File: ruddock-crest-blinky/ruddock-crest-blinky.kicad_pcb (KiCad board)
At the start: 2 copper layers, 38.1 x 45.7 mm, 35 parts, among them J1 JST PH, Q1 DMN2058UW, SW1 JS102011JCQN, SW2 PTS 647 SK38 SMTR2 LFS, U1 ATtiny85-20SU, U2 74HC595

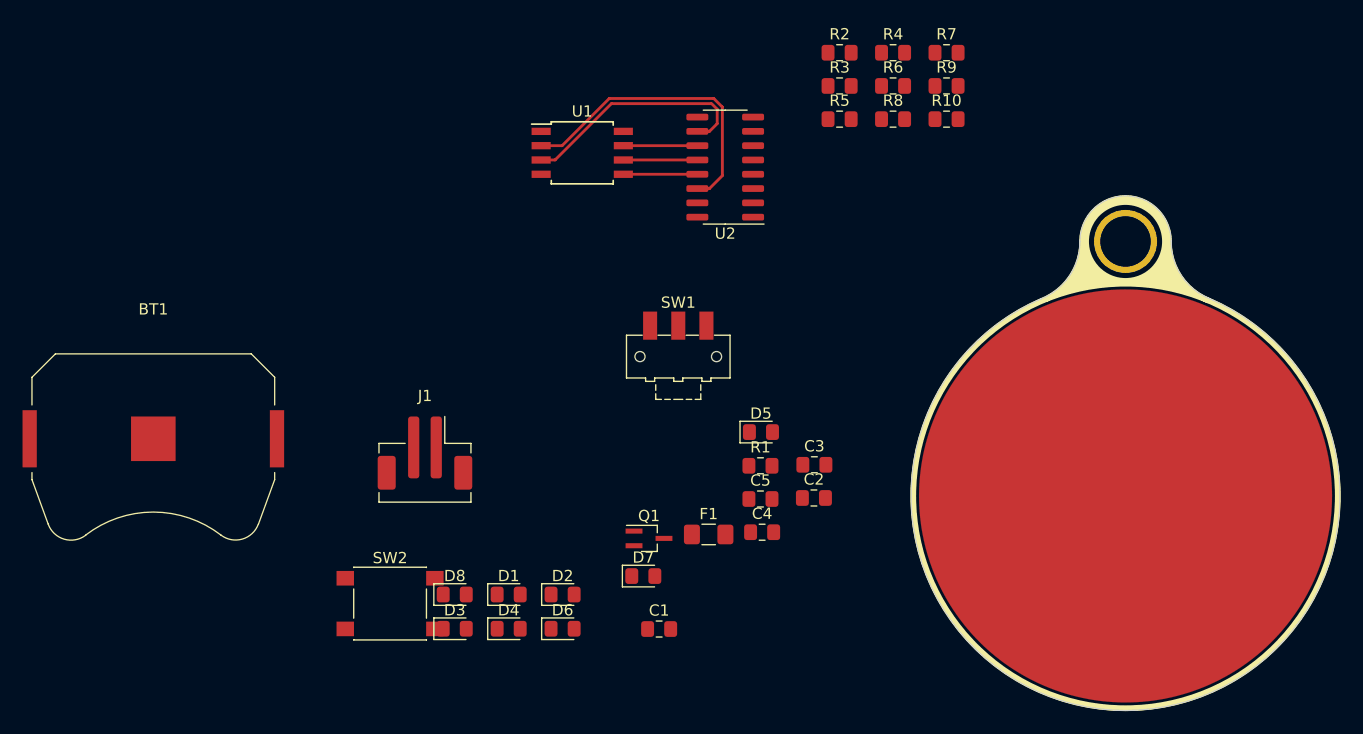
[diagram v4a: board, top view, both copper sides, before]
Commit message: Definitely not driving 8 blue LEDs off single CR2032
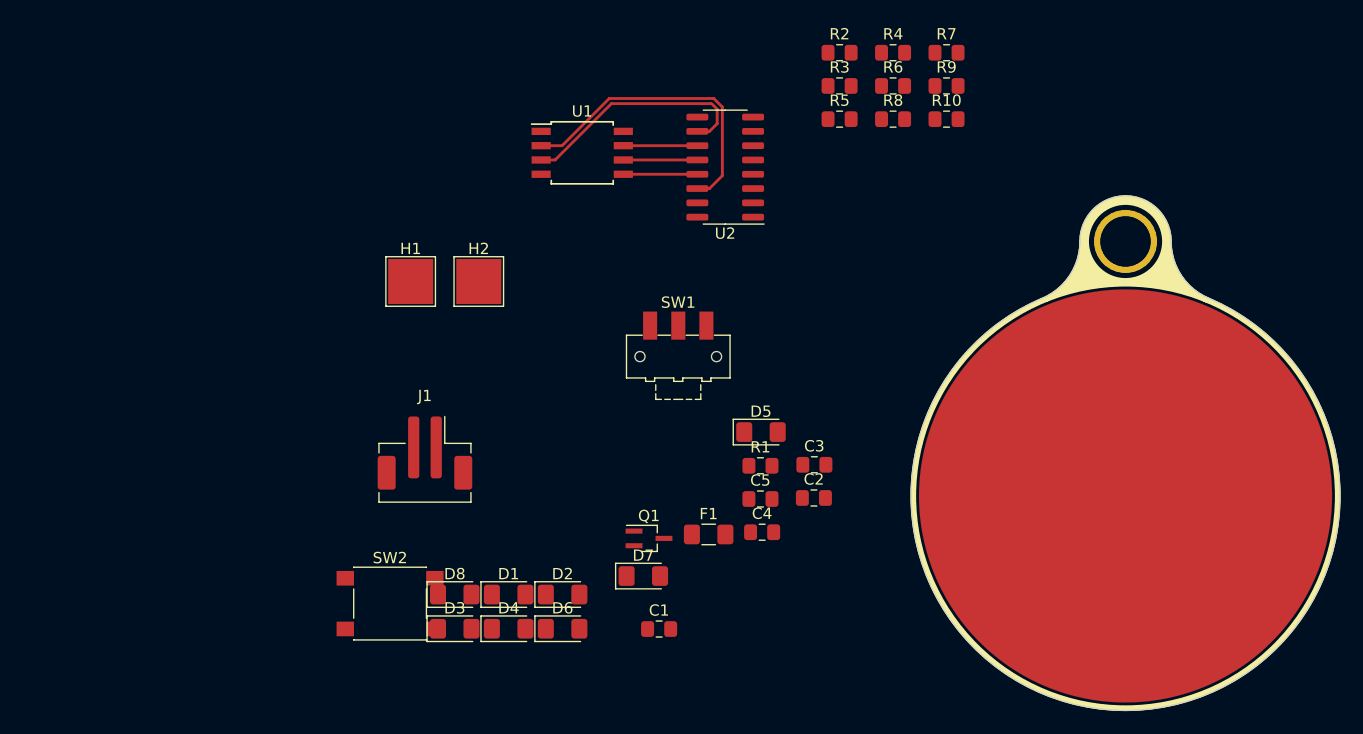
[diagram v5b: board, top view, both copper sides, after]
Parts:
- removed BT1: CR2032, Battery:BatteryHolder_Keystone_3034_1x20mm
- added H1: BAT_POS, TestPoint:TestPoint_Pad_4.0x4.0mm, F.Cu at (77.5, 88.9)
- added H2: BAT_NEG, TestPoint:TestPoint_Pad_4.0x4.0mm, F.Cu at (83.5, 88.9)
- D1, D2, D3, D4, D5, D6, D7, D8: value BLUE -> 150120BS75000; footprint LED_SMD:LED_0805_2012Metric_Pad1.15x1.40mm_HandSolder -> LED_SMD:LED_1206_3216Metric_Pad1.42x1.75mm_HandSolder
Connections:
- net Net-(BT1-Pad1) renamed /BAT+
- net Net-(BT1-Pad2) renamed /BAT-

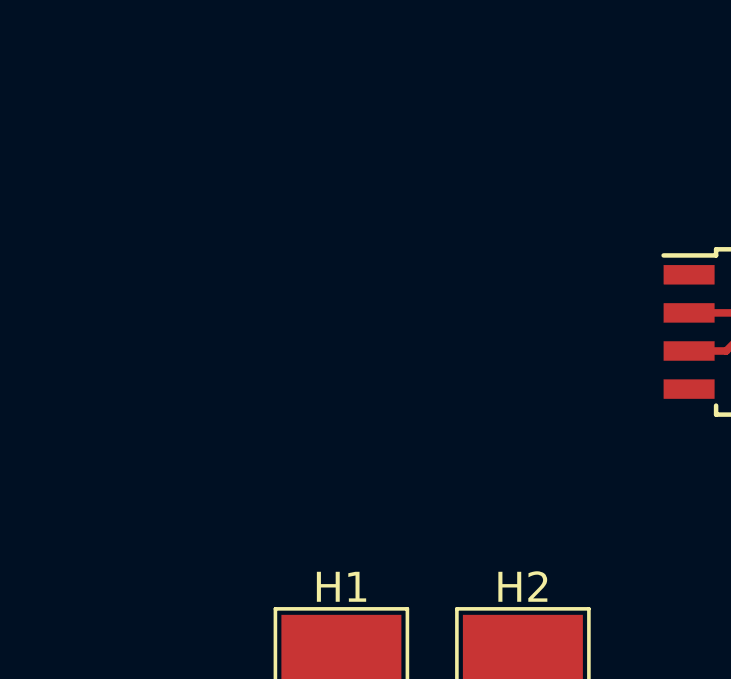
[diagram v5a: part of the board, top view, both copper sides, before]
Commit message: Add symbols for mounting hole and crest copper
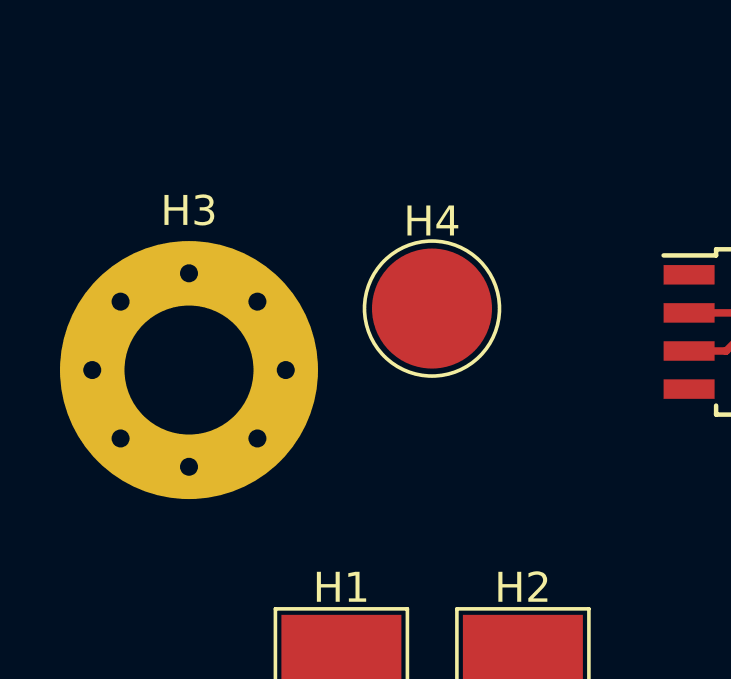
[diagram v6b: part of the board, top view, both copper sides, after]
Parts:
- added H3: KEYHOLE, MountingHole:MountingHole_4.3mm_M4_Pad_Via, F.Cu at (72.4, 78.7)
- added H4: CREST, TestPoint:TestPoint_Pad_D4.0mm, F.Cu at (80.5, 76.7)
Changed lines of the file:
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@@
     (tracks 19)
     (zones 0)
-    (modules 36)
-    (nets 31)
+    (modules 38)
+    (nets 33)
   )
   (page A)
@@
     (mod_text_size 1 1)
     (mod_text_width 0.15)
-    (pad_size 5.6 5.6)
-    (pad_drill 4.5)
+    (pad_size 7.366 7.366)
+    (pad_drill 5.334)
     (pad_to_mask_clearance 0.2)
     (solder_mask_min_width 0.25)
@@
   (net 29 /BAT+)
   (net 30 /BAT-)
+  (net 31 "Net-(H3-Pad1)")
+  (net 32 "Net-(H4-Pad1)")
   (net_class Default "This is the default net class."
     (clearance 0.2032)
@@
     (add_net "Net-(D8-Pad2)")
     (add_net "Net-(F1-Pad2)")
+    (add_net "Net-(H3-Pad1)")
+    (add_net "Net-(H4-Pad1)")
     (add_net "Net-(R1-Pad2)")
     (add_net "Net-(R2-Pad1)")
@@
     (add_net VCC)
   )
+  (module TestPoint:TestPoint_Pad_D4.0mm (layer F.Cu)
+    (at 80.49 76.69)
+    (descr "SMD pad as test Point, diameter 4.0mm")
+    (tags "test point SMD pad")
+    (attr virtual)
+    (fp_text reference H4 (at 0 -2.898) (layer F.SilkS)
+      (effects (font (size 1 1) (thickness 0.15)))
+    )
+    (fp_text value CREST (at 0 3.1) (layer F.Fab)
+      (effects (font (size 1 1) (thickness 0.15)))
+    )
+    (fp_circle (center 0 0) (end 0 2.25) (layer F.SilkS) (width 0.12))
+    (fp_circle (center 0 0) (end 2.5 0) (layer F.CrtYd) (width 0.05))
+    (fp_text user %R (at 0 -2.9) (layer F.Fab)
+      (effects (font (size 1 1) (thickness 0.15)))
+    )
+    (pad 1 smd circle (at 0 0) (size 4 4) (layers F.Cu F.Mask)
+      (net 32 "Net-(H4-Pad1)"))
+  )
+  (module MountingHole:MountingHole_4.3mm_M4_Pad_Via (layer F.Cu)
+    (at 72.39 78.74)
+    (descr "Mounting Hole 4.3mm, M4")
+    (tags "mounting hole 4.3mm m4")
+    (attr virtual)
+    (fp_text reference H3 (at 0 -5.3) (layer F.SilkS)
+      (effects (font (size 1 1) (thickness 0.15)))
+    )
+    (fp_text value KEYHOLE (at 0 5.3) (layer F.Fab)
+      (effects (font (size 1 1) (thickness 0.15)))
+    )
+    (fp_circle (center 0 0) (end 4.55 0) (layer F.CrtYd) (width 0.05))
+    (fp_circle (center 0 0) (end 4.3 0) (layer Cmts.User) (width 0.15))
+    (fp_text user %R (at 0.3 0) (layer F.Fab)
+      (effects (font (size 1 1) (thickness 0.15)))
+    )
+    (pad 1 thru_hole circle (at 2.280419 -2.280419) (size 0.9 0.9) (drill 0.6) (layers *.Cu *.Mask)
+      (net 31 "Net-(H3-Pad1)"))
+    (pad 1 thru_hole circle (at 0 -3.225) (size 0.9 0.9) (drill 0.6) (layers *.Cu *.Mask)
+      (net 31 "Net-(H3-Pad1)"))
+    (pad 1 thru_hole circle (at -2.280419 -2.280419) (size 0.9 0.9) (drill 0.6) (layers *.Cu *.Mask)
+      (net 31 "Net-(H3-Pad1)"))
+    (pad 1 thru_hole circle (at -3.225 0) (size 0.9 0.9) (drill 0.6) (layers *.Cu *.Mask)
+      (net 31 "Net-(H3-Pad1)"))
+    (pad 1 thru_hole circle (at -2.280419 2.280419) (size 0.9 0.9) (drill 0.6) (layers *.Cu *.Mask)
+      (net 31 "Net-(H3-Pad1)"))
+    (pad 1 thru_hole circle (at 0 3.225) (size 0.9 0.9) (drill 0.6) (layers *.Cu *.Mask)
+      (net 31 "Net-(H3-Pad1)"))
+    (pad 1 thru_hole circle (at 2.280419 2.280419) (size 0.9 0.9) (drill 0.6) (layers *.Cu *.Mask)
+      (net 31 "Net-(H3-Pad1)"))
+    (pad 1 thru_hole circle (at 3.225 0) (size 0.9 0.9) (drill 0.6) (layers *.Cu *.Mask)
+      (net 31 "Net-(H3-Pad1)"))
+    (pad 1 thru_hole circle (at 0 0) (size 8.6 8.6) (drill 4.3) (layers *.Cu *.Mask)
+      (net 31 "Net-(H3-Pad1)"))
+  )
   (module TestPoint:TestPoint_Pad_4.0x4.0mm (layer F.Cu)

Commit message: Add labels to MCU pins
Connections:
- net Net-(C5-Pad1) renamed /USER
- net Net-(R1-Pad2) renamed /RESET
- net Net-(U1-Pad2) renamed /SER
- net Net-(U1-Pad5) renamed /~OE
- net Net-(U1-Pad6) renamed /RCLK
- net Net-(U1-Pad7) renamed /SRCLK

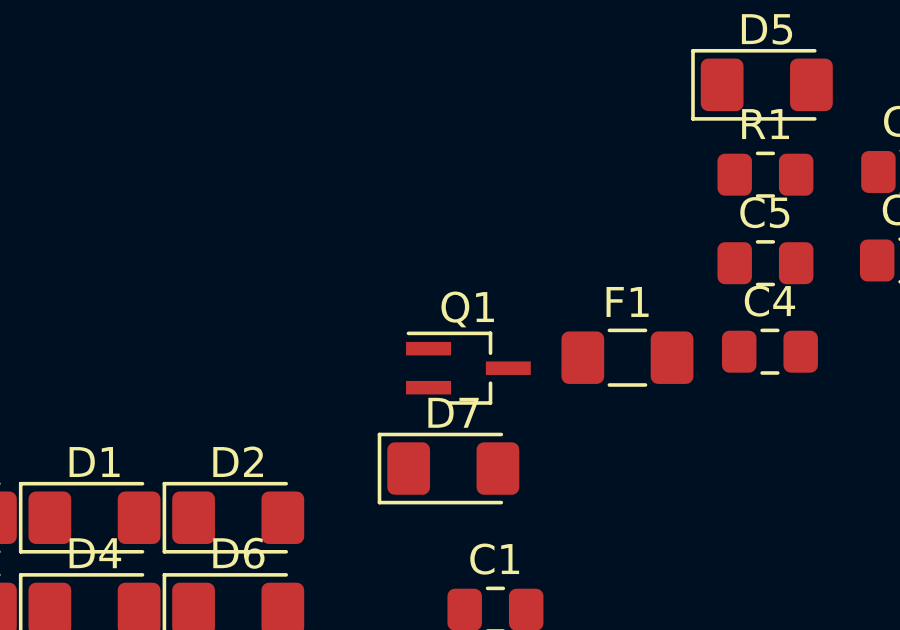
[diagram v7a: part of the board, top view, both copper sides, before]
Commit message: Replace MOSFET with SOT-23 for easier soldering
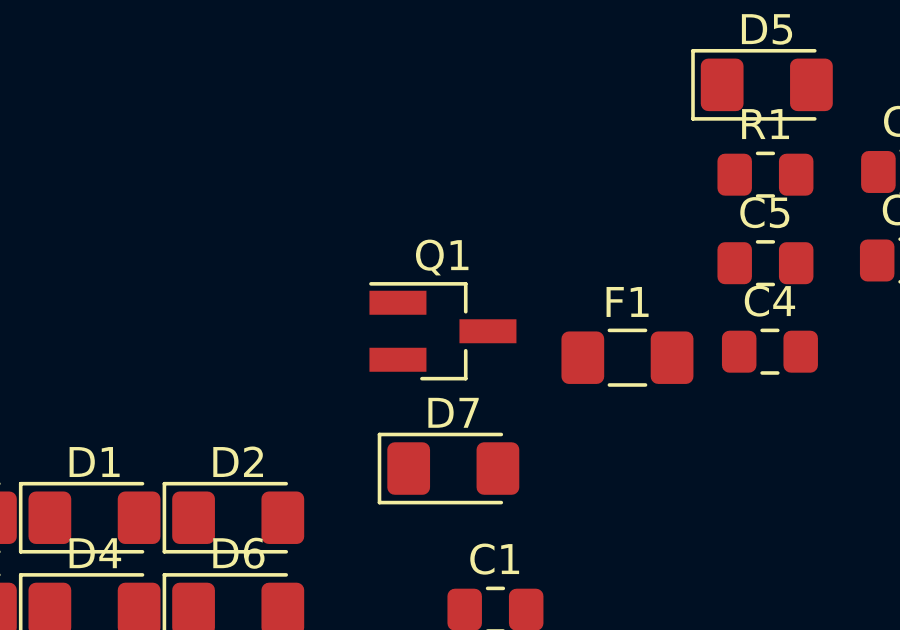
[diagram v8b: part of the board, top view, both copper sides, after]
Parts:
- Q1: value DMN2058UW -> IRFML8244; footprint Package_TO_SOT_SMD:SOT-323_SC-70_Handsoldering -> Package_TO_SOT_SMD:SOT-23_Handsoldering
- moved Q1 1.50 mm to (97.8, 110.5)
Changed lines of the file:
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@@
     (add_net VCC)
+  )
+  (module Package_TO_SOT_SMD:SOT-23_Handsoldering (layer F.Cu)
+    (at 97.79 110.49)
+    (descr "SOT-23, Handsoldering")
+    (tags SOT-23)
+    (attr smd)
+    (fp_text reference Q1 (at 0 -2.5) (layer F.SilkS)
+      (effects (font (size 1 1) (thickness 0.15)))
+    )
+    (fp_text value " IRFML8244" (at 0 2.5) (layer F.Fab)
+      (effects (font (size 1 1) (thickness 0.15)))
+    )
+    (fp_line (start 0.76 1.58) (end -0.7 1.58) (layer F.SilkS) (width 0.12))
+    (fp_line (start -0.7 1.52) (end 0.7 1.52) (layer F.Fab) (width 0.1))
+    (fp_line (start 0.7 -1.52) (end 0.7 1.52) (layer F.Fab) (width 0.1))
+    (fp_line (start -0.7 -0.95) (end -0.15 -1.52) (layer F.Fab) (width 0.1))
+    (fp_line (start -0.15 -1.52) (end 0.7 -1.52) (layer F.Fab) (width 0.1))
+    (fp_line (start -0.7 -0.95) (end -0.7 1.5) (layer F.Fab) (width 0.1))
+    (fp_line (start 0.76 -1.58) (end -2.4 -1.58) (layer F.SilkS) (width 0.12))
+    (fp_line (start -2.7 1.75) (end -2.7 -1.75) (layer F.CrtYd) (width 0.05))
+    (fp_line (start 2.7 1.75) (end -2.7 1.75) (layer F.CrtYd) (width 0.05))
+    (fp_line (start 2.7 -1.75) (end 2.7 1.75) (layer F.CrtYd) (width 0.05))
+    (fp_line (start -2.7 -1.75) (end 2.7 -1.75) (layer F.CrtYd) (width 0.05))
+    (fp_line (start 0.76 -1.58) (end 0.76 -0.65) (layer F.SilkS) (width 0.12))
+    (fp_line (start 0.76 1.58) (end 0.76 0.65) (layer F.SilkS) (width 0.12))
+    (fp_text user %R (at 0 0 90) (layer F.Fab)
+      (effects (font (size 0.5 0.5) (thickness 0.075)))
+    )
+    (pad 3 smd rect (at 1.5 0) (size 1.9 0.8) (layers F.Cu F.Paste F.Mask)
+      (net 24 /BAT-))
+    (pad 2 smd rect (at -1.5 0.95) (size 1.9 0.8) (layers F.Cu F.Paste F.Mask)
+      (net 1 GND))
+    (pad 1 smd rect (at -1.5 -0.95) (size 1.9 0.8) (layers F.Cu F.Paste F.Mask)
+      (net 2 VCC))
+    (model ${KISYS3DMOD}/Package_TO_SOT_SMD.3dshapes/SOT-23.wrl
+      (at (xyz 0 0 0))
+      (scale (xyz 1 1 1))
+      (rotate (xyz 0 0 0))
+    )
   )
   (module TestPoint:TestPoint_Pad_D4.0mm (layer F.Cu)
@@
       (at (xyz 0 0 0))
       (scale (xyz 1 1 1))
-      (rotate (xyz 0 0 0))
-    )
-  )
-  (module Package_TO_SOT_SMD:SOT-323_SC-70_Handsoldering (layer F.Cu)
-    (at 98.64 111.72103)
-    (descr "SOT-323, SC-70 Handsoldering")
-    (tags "SOT-323 SC-70 Handsoldering")
-    (attr smd)
-    (fp_text reference Q1 (at 0 -2) (layer F.SilkS)
-      (effects (font (size 1 1) (thickness 0.15)))
-    )
-    (fp_text value DMN2058UW (at 0 2.05) (layer F.Fab)
-      (effects (font (size 1 1) (thickness 0.15)))
-    )
-    (fp_line (start -0.175 -1.1) (end -0.675 -0.6) (layer F.Fab) (width 0.1))
-    (fp_line (start 0.675 1.1) (end -0.675 1.1) (layer F.Fab) (width 0.1))
-    (fp_line (start 0.675 -1.1) (end 0.675 1.1) (layer F.Fab) (width 0.1))
-    (fp_line (start -0.675 -0.6) (end -0.675 1.1) (layer F.Fab) (width 0.1))
-    (fp_line (start 0.675 -1.1) (end -0.175 -1.1) (layer F.Fab) (width 0.1))
-    (fp_line (start -0.675 1.16) (end 0.735 1.16) (layer F.SilkS) (width 0.12))
-    (fp_line (start 0.735 -1.16) (end -2 -1.16) (layer F.SilkS) (width 0.12))
-    (fp_line (start -2.4 1.3) (end -2.4 -1.3) (layer F.CrtYd) (width 0.05))
-    (fp_line (start -2.4 -1.3) (end 2.4 -1.3) (layer F.CrtYd) (width 0.05))
-    (fp_line (start 2.4 -1.3) (end 2.4 1.3) (layer F.CrtYd) (width 0.05))
-    (fp_line (start 2.4 1.3) (end -2.4 1.3) (layer F.CrtYd) (width 0.05))
-    (fp_line (start 0.735 -1.17) (end 0.735 -0.5) (layer F.SilkS) (width 0.12))
-    (fp_line (start 0.735 0.5) (end 0.735 1.16) (layer F.SilkS) (width 0.12))
-    (fp_text user %R (at 0 0 90) (layer F.Fab)
-      (effects (font (size 0.5 0.5) (thickness 0.075)))
-    )
-    (pad 3 smd rect (at 1.33 0 270) (size 0.45 1.5) (layers F.Cu F.Paste F.Mask)
-      (net 24 /BAT-))
-    (pad 2 smd rect (at -1.33 0.65 270) (size 0.45 1.5) (layers F.Cu F.Paste F.Mask)
-      (net 1 GND))
-    (pad 1 smd rect (at -1.33 -0.65 270) (size 0.45 1.5) (layers F.Cu F.Paste F.Mask)
-      (net 2 VCC))
-    (model ${KISYS3DMOD}/Package_TO_SOT_SMD.3dshapes/SOT-323_SC-70.wrl
-      (at (xyz 0 0 0))
-      (scale (xyz 1 1 1))
